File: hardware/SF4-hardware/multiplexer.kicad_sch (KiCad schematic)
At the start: 2 parts, among them U5 MCP6004, U6 MCP6004

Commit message: Modified simulation and harware files
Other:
- note added: "Connections into multiplexer"
- note added: "Op-amp power and unused op-amps"
- note added: "Shorting Buffers"
- moved on the sheet: U5A, U5B, U5C, U5D, U6A, U6B

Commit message: Added kicad backup files
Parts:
- added R37, R38: 22k, symbol Device:R
- added U6: MCP6004, symbol Amplifier_Operational:MCP6004
- U5: value MCP6004 -> LM324; symbol Amplifier_Operational:MCP6004 -> Amplifier_Operational:LM324
- U7: renamed from U6; value MCP6004 -> LM324; symbol Amplifier_Operational:MCP6004 -> Amplifier_Operational:LM324
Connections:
- net +5V: now also R37.1, U6.4 (V+); no longer U5.4 (V+), U7.4 (V+)
- net GND: now also R38.2, U6.11 (V-); no longer U5.11 (V-), U7.11 (V-)
- new net: R37.2, R38.1, U6.3 (+)
- new net +5VA: U5.4 (V+), U7.4 (V+)
- new net -5VA: U5.11 (V-), U7.11 (V-)
- new net vref: U6.1, U6.2 (-)
- no-connect marks 6 -> 15
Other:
- moved on the sheet: U7C, U7D

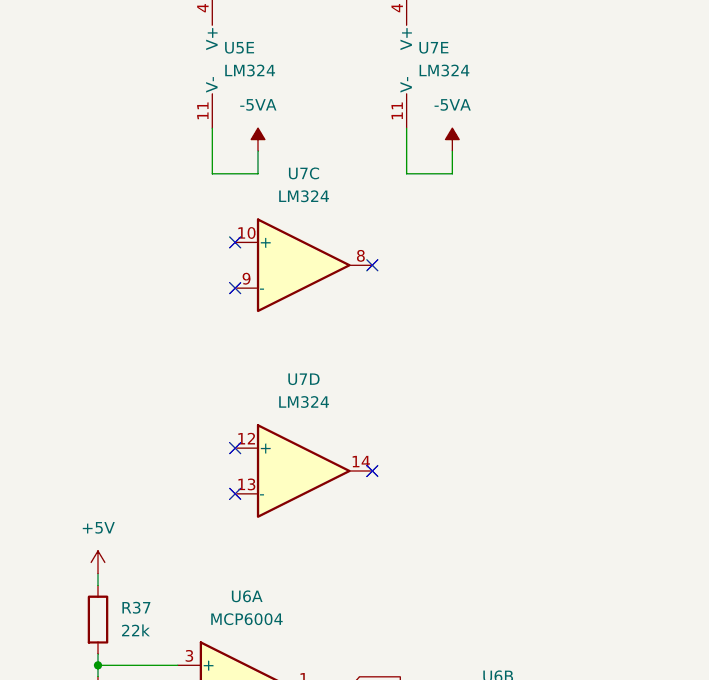
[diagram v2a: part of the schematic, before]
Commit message: Added new ECG circuit
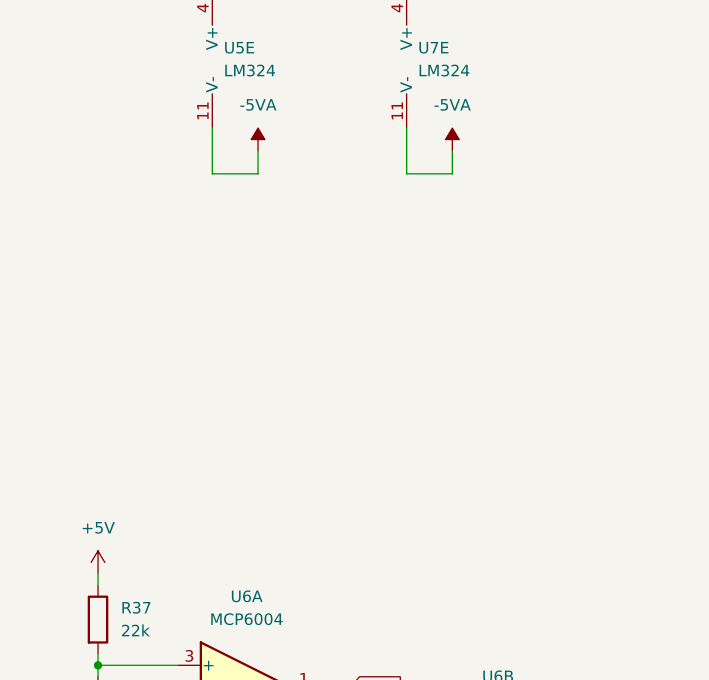
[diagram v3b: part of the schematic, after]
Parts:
- removed unit 4 of U7
- removed unit 3 of U7
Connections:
- no-connect marks 15 -> 9
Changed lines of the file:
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@@
-	)
-	(no_connect
-		(at 36.83 153.67)
 	)
 	(no_connect
@@
 	)
 	(no_connect
-		(at 36.83 148.59)
-	)
-	(no_connect
-		(at 36.83 125.73)
-	)
-	(no_connect
 		(at 120.65 181.61)
-	)
-	(no_connect
-		(at 36.83 130.81)
-	)
-	(no_connect
-		(at 52.07 151.13)
 	)
 	(no_connect
@@
 	(no_connect
 		(at 58.42 186.69)
-	)
-	(no_connect
-		(at 52.07 128.27)
 	)
 	(wire
@@
 	(symbol
 		(lib_id "Amplifier_Operational:LM324")
-		(at 44.45 151.13 0)
-		(unit 4)
-		(exclude_from_sim no)
-		(in_bom yes)
-		(on_board yes)
-		(dnp no)
-		(fields_autoplaced yes)
-		(property "Reference" "U7"
-			(at 44.45 140.97 0)
-			(effects
-				(font
-					(size 1.27 1.27)
-				)
-			)
-		)
-		(property "Value" "LM324"
-			(at 44.45 143.51 0)
-			(effects
-				(font
-					(size 1.27 1.27)
-				)
-			)
-		)
-		(property "Footprint" ""
-			(at 43.18 148.59 0)
-			(effects
-				(font
-					(size 1.27 1.27)
-				)
-				(hide yes)
-			)
-		)
-		(property "Datasheet" "http://www.ti.com/lit/ds/symlink/lm2902-n.pdf"
-			(at 45.72 146.05 0)
-			(effects
-				(font
-					(size 1.27 1.27)
-				)
-				(hide yes)
-			)
-		)
-		(property "Description" "Low-Power, Quad-Operational Amplifiers, DIP-14/SOIC-14/SSOP-14"
-			(at 44.45 151.13 0)
-			(effects
-				(font
-					(size 1.27 1.27)
-				)
-				(hide yes)
-			)
-		)
-		(pin "4"
-		)
-		(pin "3"
-		)
-		(pin "13"
-		)
-		(pin "8"
-		)
-		(pin "12"
-		)
-		(pin "2"
-		)
-		(pin "7"
-		)
-		(pin "14"
-		)
-		(pin "1"
-		)
-		(pin "5"
-		)
-		(pin "11"
-		)
-		(pin "6"
-		)
-		(pin "9"
-		)
-		(pin "10"
-		)
-		(instances
-			(project "SF4-hardware"
-				(path "/ef5111bd-e8db-4b6d-9a36-6e7b6428b384/771a61c7-b176-4389-83a8-1da0552c5a31"
-					(reference "U7")
-					(unit 4)
-				)
-			)
-		)
-	)
-	(symbol
-		(lib_id "Amplifier_Operational:LM324")
 		(at 194.31 125.73 0)
 		(unit 2)
@@
 					(unit 3)
 				)
-			)
-		)
-	)
-	(symbol
-		(lib_id "Amplifier_Operational:LM324")
-		(at 44.45 128.27 0)
-		(unit 3)
-		(exclude_from_sim no)
-		(in_bom yes)
-		(on_board yes)
-		(dnp no)
-		(fields_autoplaced yes)
-		(property "Reference" "U7"
-			(at 44.45 118.11 0)
-			(effects
-				(font
-					(size 1.27 1.27)
-				)
-			)
-		)
-		(property "Value" "LM324"
-			(at 44.45 120.65 0)
-			(effects
-				(font
-					(size 1.27 1.27)
-				)
-			)
-		)
-		(property "Footprint" ""
-			(at 43.18 125.73 0)
-			(effects
-				(font
-					(size 1.27 1.27)
-				)
-				(hide yes)
-			)
-		)
-		(property "Datasheet" "http://www.ti.com/lit/ds/symlink/lm2902-n.pdf"
-			(at 45.72 123.19 0)
-			(effects
-				(font
-					(size 1.27 1.27)
-				)
-				(hide yes)
-			)
-		)
-		(property "Description" "Low-Power, Quad-Operational Amplifiers, DIP-14/SOIC-14/SSOP-14"
-			(at 44.45 128.27 0)
-			(effects
-				(font
-					(size 1.27 1.27)
-				)
-				(hide yes)
-			)
-		)
-		(pin "4"
-		)
-		(pin "3"
-		)
-		(pin "13"
-		)
-		(pin "8"
-		)
-		(pin "12"
-		)
-		(pin "2"
-		)
-		(pin "7"
-		)
-		(pin "14"
-		)
-		(pin "1"
-		)
-		(pin "5"
-		)
-		(pin "11"
-		)
-		(pin "6"
-		)
-		(pin "9"
-		)
-		(pin "10"
-		)
-		(instances
-			(project "SF4-hardware"
-				(path "/ef5111bd-e8db-4b6d-9a36-6e7b6428b384/771a61c7-b176-4389-83a8-1da0552c5a31"
-					(reference "U7")
-					(unit 3)
-				)

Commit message: Added changes to hardware
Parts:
- renumbered R37 to R1, R38 to R2, U5 to U2, U6 to U3, U7 to U4
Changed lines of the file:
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@@
 		(dnp no)
 		(fields_autoplaced yes)
-		(property "Reference" "#PWR024"
+		(property "Reference" "#PWR012"
 			(at 34.29 99.06 0)
 			(effects
@@
 			(project "SF4-hardware"
 				(path "/ef5111bd-e8db-4b6d-9a36-6e7b6428b384/771a61c7-b176-4389-83a8-1da0552c5a31"
-					(reference "#PWR024")
+					(reference "#PWR012")
 					(unit 1)
 				)
@@
 		(dnp no)
 		(fields_autoplaced yes)
-		(property "Reference" "U7"
+		(property "Reference" "U4"
 			(at 194.31 115.57 0)
 			(effects
@@
 			(project "SF4-hardware"
 				(path "/ef5111bd-e8db-4b6d-9a36-6e7b6428b384/771a61c7-b176-4389-83a8-1da0552c5a31"
-					(reference "U7")
+					(reference "U4")
 					(unit 2)
 				)
@@
 		(dnp no)
 		(fields_autoplaced yes)
-		(property "Reference" "U7"
+		(property "Reference" "U4"
 			(at 57.15 104.1399 0)
 			(effects
@@
 			(project "SF4-hardware"
 				(path "/ef5111bd-e8db-4b6d-9a36-6e7b6428b384/771a61c7-b176-4389-83a8-1da0552c5a31"
-					(reference "U7")
+					(reference "U4")
 					(unit 5)
 				)
@@
 		(dnp no)
 		(fields_autoplaced yes)
-		(property "Reference" "R37"
+		(property "Reference" "R1"
 			(at 24.13 166.3699 0)
 			(effects
@@
 			(project "SF4-hardware"
 				(path "/ef5111bd-e8db-4b6d-9a36-6e7b6428b384/771a61c7-b176-4389-83a8-1da0552c5a31"
-					(reference "R37")
+					(reference "R1")
 					(unit 1)
 				)
@@
 		(dnp no)
 		(fields_autoplaced yes)
-		(property "Reference" "U6"
+		(property "Reference" "U3"
 			(at 128.27 173.99 0)
 			(effects
@@
 			(project "SF4-hardware"
 				(path "/ef5111bd-e8db-4b6d-9a36-6e7b6428b384/771a61c7-b176-4389-83a8-1da0552c5a31"
-					(reference "U6")
+					(reference "U3")
 					(unit 4)
 				)
@@
 		(dnp no)
 		(fields_autoplaced yes)
-		(property "Reference" "U7"
+		(property "Reference" "U4"
 			(at 194.31 95.25 0)
 			(effects
@@
 			(project "SF4-hardware"
 				(path "/ef5111bd-e8db-4b6d-9a36-6e7b6428b384/771a61c7-b176-4389-83a8-1da0552c5a31"
-					(reference "U7")
+					(reference "U4")
 					(unit 1)
 				)
@@
 		(dnp no)
 		(fields_autoplaced yes)
-		(property "Reference" "U5"
+		(property "Reference" "U2"
 			(at 35.56 104.1399 0)
 			(effects
@@
 			(project "SF4-hardware"
 				(path "/ef5111bd-e8db-4b6d-9a36-6e7b6428b384/771a61c7-b176-4389-83a8-1da0552c5a31"
-					(reference "U5")
+					(reference "U2")
 					(unit 5)
 				)
@@
 		(dnp no)
 		(fields_autoplaced yes)
-		(property "Reference" "U6"
+		(property "Reference" "U3"
 			(at 161.29 181.6099 0)
 			(effects
@@
 			(project "SF4-hardware"
 				(path "/ef5111bd-e8db-4b6d-9a36-6e7b6428b384/771a61c7-b176-4389-83a8-1da0552c5a31"
-					(reference "U6")
+					(reference "U3")
 					(unit 5)
 				)
@@
 		(dnp no)
 		(fields_autoplaced yes)
-		(property "Reference" "U5"
+		(property "Reference" "U2"
 			(at 231.14 57.15 0)
 			(effects
@@
 			(project "SF4-hardware"
 				(path "/ef5111bd-e8db-4b6d-9a36-6e7b6428b384/771a61c7-b176-4389-83a8-1da0552c5a31"
-					(reference "U5")
+					(reference "U2")
 					(unit 4)
 				)
@@
 		(dnp no)
 		(fields_autoplaced yes)
-		(property "Reference" "#PWR027"
+		(property "Reference" "#PWR015"
 			(at 60.96 119.38 0)
 			(effects
@@
 			(project "SF4-hardware"
 				(path "/ef5111bd-e8db-4b6d-9a36-6e7b6428b384/771a61c7-b176-4389-83a8-1da0552c5a31"
-					(reference "#PWR027")
+					(reference "#PWR015")
 					(unit 1)
 				)
@@
 		(dnp no)
 		(fields_autoplaced yes)
-		(property "Reference" "U5"
+		(property "Reference" "U2"
 			(at 140.97 57.15 0)
 			(effects
@@
 			(project "SF4-hardware"
 				(path "/ef5111bd-e8db-4b6d-9a36-6e7b6428b384/771a61c7-b176-4389-83a8-1da0552c5a31"
-					(reference "U5")
+					(reference "U2")
 					(unit 2)
 				)
@@
 		(dnp no)
 		(fields_autoplaced yes)
-		(property "Reference" "U5"
+		(property "Reference" "U2"
 			(at 140.97 39.37 0)
 			(effects
@@
 			(project "SF4-hardware"
 				(path "/ef5111bd-e8db-4b6d-9a36-6e7b6428b384/771a61c7-b176-4389-83a8-1da0552c5a31"
-					(reference "U5")
+					(reference "U2")
 					(unit 1)
 				)
@@
 		(dnp no)
 		(fields_autoplaced yes)
-		(property "Reference" "#PWR023"
+		(property "Reference" "#PWR011"
 			(at 21.59 189.23 0)
 			(effects
@@
 			(project "SF4-hardware"
 				(path "/ef5111bd-e8db-4b6d-9a36-6e7b6428b384/771a61c7-b176-4389-83a8-1da0552c5a31"
-					(reference "#PWR023")
+					(reference "#PWR011")
 					(unit 1)
 				)
@@
 		(dnp no)
 		(fields_autoplaced yes)
-		(property "Reference" "#PWR025"
+		(property "Reference" "#PWR013"
 			(at 39.37 119.38 0)
 			(effects
@@
 			(project "SF4-hardware"
 				(path "/ef5111bd-e8db-4b6d-9a36-6e7b6428b384/771a61c7-b176-4389-83a8-1da0552c5a31"
-					(reference "#PWR025")
+					(reference "#PWR013")
 					(unit 1)
 				)
@@
 		(dnp no)
 		(fields_autoplaced yes)
-		(property "Reference" "U6"
+		(property "Reference" "U3"
 			(at 100.33 173.99 0)
 			(effects
@@
 			(project "SF4-hardware"
 				(path "/ef5111bd-e8db-4b6d-9a36-6e7b6428b384/771a61c7-b176-4389-83a8-1da0552c5a31"
-					(reference "U6")
+					(reference "U3")
 					(unit 3)
 				)
@@
 		(dnp no)
 		(fields_autoplaced yes)
-		(property "Reference" "#PWR026"
+		(property "Reference" "#PWR014"
 			(at 55.88 99.06 0)
 			(effects
@@
 			(project "SF4-hardware"
 				(path "/ef5111bd-e8db-4b6d-9a36-6e7b6428b384/771a61c7-b176-4389-83a8-1da0552c5a31"
-					(reference "#PWR026")
+					(reference "#PWR014")
 					(unit 1)
 				)
@@
 		(dnp no)
 		(fields_autoplaced yes)
-		(property "Reference" "U6"
+		(property "Reference" "U3"
 			(at 38.1 165.1 0)
 			(effects
@@
 			(project "SF4-hardware"
 				(path "/ef5111bd-e8db-4b6d-9a36-6e7b6428b384/771a61c7-b176-4389-83a8-1da0552c5a31"
-					(reference "U6")
+					(reference "U3")
 					(unit 1)
 				)
@@
 		(dnp no)
 		(fields_autoplaced yes)
-		(property "Reference" "U5"
+		(property "Reference" "U2"
 			(at 231.14 39.37 0)
 			(effects
@@
 			(project "SF4-hardware"
 				(path "/ef5111bd-e8db-4b6d-9a36-6e7b6428b384/771a61c7-b176-4389-83a8-1da0552c5a31"
-					(reference "U5")
+					(reference "U2")
 					(unit 3)
 				)
@@
 		(dnp no)
 		(fields_autoplaced yes)
-		(property "Reference" "R38"
+		(property "Reference" "R2"
 			(at 24.13 176.5299 0)
 			(effects
@@
 			(project "SF4-hardware"
 				(path "/ef5111bd-e8db-4b6d-9a36-6e7b6428b384/771a61c7-b176-4389-83a8-1da0552c5a31"
-					(reference "R38")
+					(reference "R2")
 					(unit 1)
 				)
@@
 		(dnp no)
 		(fields_autoplaced yes)
-		(property "Reference" "U6"
+		(property "Reference" "U3"
 			(at 66.04 173.99 0)
 			(effects
@@
 			(project "SF4-hardware"
 				(path "/ef5111bd-e8db-4b6d-9a36-6e7b6428b384/771a61c7-b176-4389-83a8-1da0552c5a31"
-					(reference "U6")
+					(reference "U3")
 					(unit 2)
 				)
@@
 		(dnp no)
 		(fields_autoplaced yes)
-		(property "Reference" "#PWR028"
+		(property "Reference" "#PWR016"
 			(at 160.02 176.53 0)
 			(effects
@@
 			(project "SF4-hardware"
 				(path "/ef5111bd-e8db-4b6d-9a36-6e7b6428b384/771a61c7-b176-4389-83a8-1da0552c5a31"
-					(reference "#PWR028")
+					(reference "#PWR016")
 					(unit 1)
 				)
@@
 		(dnp no)
 		(fields_autoplaced yes)
-		(property "Reference" "#PWR022"
+		(property "Reference" "#PWR010"
 			(at 21.59 166.37 0)
 			(effects
@@
 			(project "SF4-hardware"
 				(path "/ef5111bd-e8db-4b6d-9a36-6e7b6428b384/771a61c7-b176-4389-83a8-1da0552c5a31"
-					(reference "#PWR022")
+					(reference "#PWR010")
 					(unit 1)
 				)
@@
 		(dnp no)
 		(fields_autoplaced yes)
-		(property "Reference" "#PWR029"
+		(property "Reference" "#PWR017"
 			(at 160.02 198.12 0)
 			(effects
@@
 			(project "SF4-hardware"
 				(path "/ef5111bd-e8db-4b6d-9a36-6e7b6428b384/771a61c7-b176-4389-83a8-1da0552c5a31"
-					(reference "#PWR029")
+					(reference "#PWR017")
 					(unit 1)
 				)
